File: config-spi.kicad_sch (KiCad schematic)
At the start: 29 parts, among them J3001 PinHeader_2x7_P2mm_SMD_Shroud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, Q3001 BSS138PW, Q3002 BSS138PW, SW3001 SW_KMR211NGLFS_SMD, SW3002 CVS-03B, U3001 S25FL128SAGNFI000, U3002 XC7K160T-FFG676

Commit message: Bump revision to 1.0.0
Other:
- title: LPDDR5 Test Board -> SO-DIMM DDR5 Tester

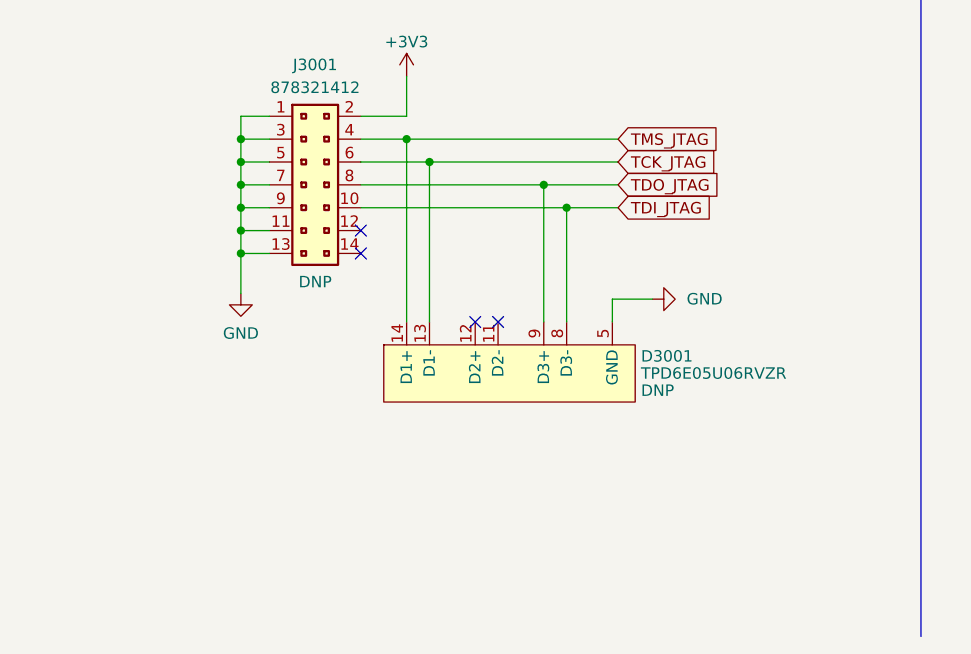
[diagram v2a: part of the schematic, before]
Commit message: Connect RFU, start improving interfaces and supply sheet, unify ESD protection
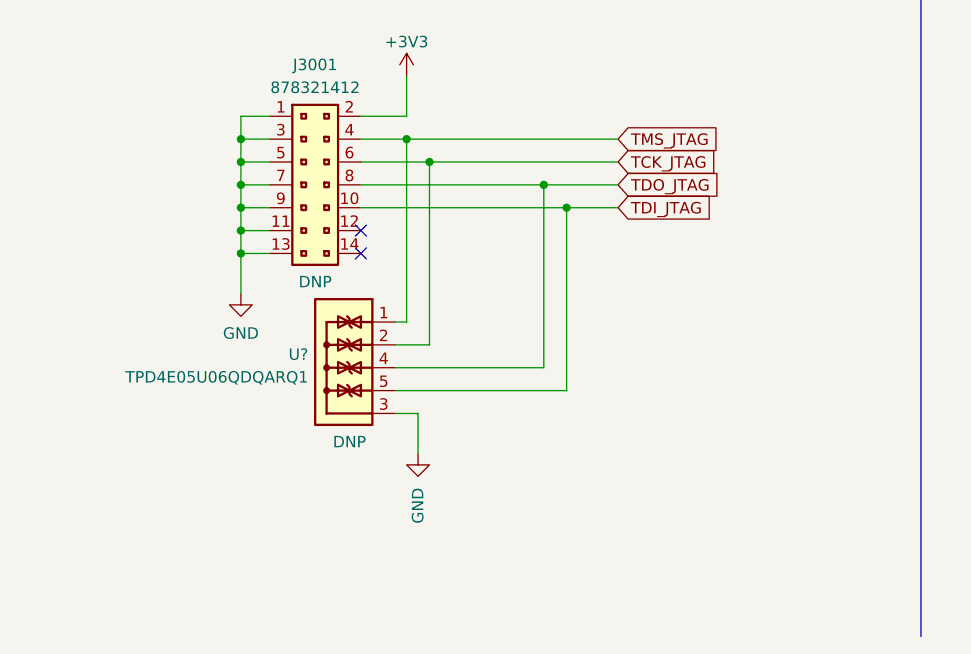
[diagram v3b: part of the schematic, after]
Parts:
- removed D3001: TPD6E05U06RVZR, sodimm-ddr5-tester-footprints:USON-14_3.5X1.3X0.5mm_P0.5mm, symbol sodimm-ddr5-tester:TPD6E05U06RVZR
- added U?: TPD4E05U06QDQARQ1, antmicro-footprints:USON-10_2.5x1mm_P0.5mm, symbol antmicroTVSDiodes:TPD4E05U06QDQARQ1
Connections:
- net GND: now also U?.3, U?.8
- net TCK_JTAG: now also U?.2, U?.9
- net TDI_JTAG: now also U?.5, U?.6
- net TDO_JTAG: now also U?.4, U?.7
- net TMS_JTAG: now also U?.1, U?.10
- no-connect marks 4 -> 2
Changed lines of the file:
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@@
   )
   (no_connect (at 50.165 242.57))
-  (no_connect (at 62.865 250.19))
-  (no_connect (at 65.405 250.19))
   (no_connect (at 50.165 240.03))
   (wire (pts (xy 111.125 88.9) (xy 111.125 92.075))
@@
     (stroke (width 0) (type default) (color 0 0 0 0))
   )
-  (wire (pts (xy 73.025 250.19) (xy 73.025 237.49))
+  (wire (pts (xy 73.025 237.49) (xy 73.025 257.81))
     (stroke (width 0) (type default) (color 0 0 0 0))
   )
@@
     (stroke (width 0) (type default) (color 0 0 0 0))
   )
-  (wire (pts (xy 57.785 250.19) (xy 57.785 232.41))
+  (wire (pts (xy 57.785 232.41) (xy 57.785 252.73))
     (stroke (width 0) (type default) (color 0 0 0 0))
   )
@@
     (stroke (width 0) (type default) (color 0 0 0 0))
   )
-  (wire (pts (xy 70.485 250.19) (xy 70.485 234.95))
+  (wire (pts (xy 70.485 234.95) (xy 70.485 255.27))
     (stroke (width 0) (type default) (color 0 0 0 0))
   )
@@
     (stroke (width 0) (type default) (color 0 0 0 0))
   )
-  (wire (pts (xy 78.105 247.65) (xy 82.55 247.65))
+  (wire (pts (xy 56.515 260.35) (xy 56.515 264.795))
     (stroke (width 0) (type default) (color 0 0 0 0))
   )
@@
     (stroke (width 0) (type default) (color 0 0 0 0))
   )
+  (wire (pts (xy 53.975 255.27) (xy 70.485 255.27))
+    (stroke (width 0) (type default) (color 0 0 0 0))
+  )
   (wire (pts (xy 50.165 229.87) (xy 55.245 229.87))
     (stroke (width 0) (type default) (color 0 0 0 0))
@@
     (stroke (width 0) (type default) (color 0 0 0 0))
   )
+  (wire (pts (xy 53.975 257.81) (xy 73.025 257.81))
+    (stroke (width 0) (type default) (color 0 0 0 0))
+  )
   (wire (pts (xy 128.905 88.9) (xy 128.905 92.075))
     (stroke (width 0) (type default) (color 0 0 0 0))
@@
     (stroke (width 0) (type default) (color 0 0 0 0))
   )
+  (wire (pts (xy 53.975 252.73) (xy 57.785 252.73))
+    (stroke (width 0) (type default) (color 0 0 0 0))
+  )
   (wire (pts (xy 224.79 258.445) (xy 252.095 258.445))
     (stroke (width 0) (type default) (color 0 0 0 0))
@@
     (stroke (width 0) (type default) (color 0 0 0 0))
   )
+  (wire (pts (xy 53.975 250.19) (xy 55.245 250.19))
+    (stroke (width 0) (type default) (color 0 0 0 0))
+  )
   (wire (pts (xy 73.025 100.965) (xy 73.025 102.87))
     (stroke (width 0) (type default) (color 0 0 0 0))
@@
     (stroke (width 0) (type default) (color 0 0 0 0))
   )
-  (wire (pts (xy 78.105 250.19) (xy 78.105 247.65))
+  (wire (pts (xy 53.975 260.35) (xy 56.515 260.35))
     (stroke (width 0) (type default) (color 0 0 0 0))
   )
@@
     (pin "1")
   )
-  (symbol (lib_id "sodimm-ddr5-tester:TPD6E05U06RVZR") (at 55.245 250.19 90) (mirror x) (unit 1)
-    (in_bom yes) (on_board yes)
-    (property "Reference" "D3001" (id 0) (at 81.28 254 90)
-      (effects (font (size 1.27 1.27)) (justify right))
-    )
-    (property "Value" "TPD6E05U06RVZR" (id 1) (at 81.28 255.905 90)
-      (effects (font (size 1.27 1.27) (thickness 0.15)) (justify right))
-    )
-    (property "Footprint" "sodimm-ddr5-tester-footprints:USON-14_3.5X1.3X0.5mm_P0.5mm" (id 2) (at 60.325 273.05 0)
-      (effects (font (size 1.27 1.27) (thickness 0.15)) (justify left bottom) hide)
-    )
-    (property "Datasheet" "http://www.ti.com/lit/ds/symlink/tpd6e05u06.pdf" (id 3) (at 62.865 273.05 0)
-      (effects (font (size 1.27 1.27) (thickness 0.15)) (justify left bottom) hide)
-    )
-    (property "MPN" "TPD6E05U06RVZR" (id 4) (at 65.405 273.05 0)
-      (effects (font (size 1.27 1.27) (thickness 0.15)) (justify left bottom) hide)
-    )
-    (property "Manufacturer" "Texas Instruments" (id 5) (at 67.945 273.05 0)
-      (effects (font (size 1.27 1.27) (thickness 0.15)) (justify left bottom) hide)
-    )
-    (property "Author" "Antmicro" (id 6) (at 70.485 273.05 0)
-      (effects (font (size 1.27 1.27) (thickness 0.15)) (justify left bottom) hide)
-    )
-    (property "License" "Apache-2.0" (id 7) (at 73.025 273.05 0)
-      (effects (font (size 1.27 1.27) (thickness 0.15)) (justify left bottom) hide)
-    )
-    (property "DNP" "DNP" (id 8) (at 81.28 257.81 90)
-      (effects (font (size 1.27 1.27)) (justify right))
-    )
-    (pin "1")
-    (pin "2")
-    (pin "3")
-    (pin "4")
-    (pin "6")
-    (pin "7")
-    (pin "10")
-    (pin "11")
-    (pin "12")
-    (pin "13")
-    (pin "14")
-    (pin "5")
-    (pin "8")
-    (pin "9")
-  )
-  (symbol (lib_id "sodimm-ddr5-tester:GND") (at 82.55 247.65 90) (unit 1)
+  (symbol (lib_id "sodimm-ddr5-tester:GND") (at 56.515 264.795 0) (unit 1)
     (in_bom yes) (on_board yes) (fields_autoplaced)
-    (property "Reference" "#PWR03004" (id 0) (at 88.9 247.65 0)
+    (property "Reference" "#PWR03004" (id 0) (at 56.515 271.145 0)
       (effects (font (size 1.27 1.27)) hide)
     )
-    (property "Value" "GND" (id 1) (at 86.36 247.6499 90)
+    (property "Value" "GND" (id 1) (at 56.5151 268.605 90)
       (effects (font (size 1.27 1.27)) (justify right))
     )
-    (property "Footprint" "" (id 2) (at 82.55 247.65 0)
+    (property "Footprint" "" (id 2) (at 56.515 264.795 0)
       (effects (font (size 1.27 1.27)) hide)
     )
-    (property "Datasheet" "" (id 3) (at 82.55 247.65 0)
+    (property "Datasheet" "" (id 3) (at 56.515 264.795 0)
       (effects (font (size 1.27 1.27)) hide)
     )
-    (property "Author" "Antmicro" (id 4) (at 90.17 238.76 0)
+    (property "Author" "Antmicro" (id 4) (at 65.405 272.415 0)
       (effects (font (size 1.27 1.27) (thickness 0.15)) (justify left bottom) hide)
     )
-    (property "License" "Apache-2.0" (id 5) (at 92.71 238.76 0)
+    (property "License" "Apache-2.0" (id 5) (at 65.405 274.955 0)
       (effects (font (size 1.27 1.27) (thickness 0.15)) (justify left bottom) hide)
     )
@@
     (pin "2")
   )
+  (symbol (lib_id "antmicroTVSDiodes:TPD4E05U06QDQARQ1") (at 53.975 250.19 0) (mirror y) (unit 1)
+    (in_bom yes) (on_board yes)
+    (property "Reference" "U?" (id 0) (at 44.323 253.8044 0)
+      (effects (font (size 1.27 1.27) (thickness 0.15)) (justify left))
+    )
+    (property "Value" "TPD4E05U06QDQARQ1" (id 1) (at 44.323 256.3281 0)
+      (effects (font (size 1.27 1.27) (thickness 0.15)) (justify left))
+    )
+    (property "Footprint" "antmicro-footprints:USON-10_2.5x1mm_P0.5mm" (id 2) (at 29.845 255.27 0)
+      (effects (font (size 1.27 1.27) (thickness 0.15)) (justify left bottom) hide)
+    )
+    (property "Datasheet" "https://www.ti.com/lit/ds/symlink/tpd4e05u06-q1.pdf?HQS=dis-mous-null-mousermode-dsf-pf-null-wwe&ts=1663591265741&ref_url=https%253A%252F%252Fwww.mouser.com%252F" (id 3) (at 29.845 257.81 0)
+      (effects (font (size 1.27 1.27) (thickness 0.15)) (justify left bottom) hide)
+    )
+    (property "Manufacturer" "Texas Instruments" (id 4) (at 29.845 260.35 0)
+      (effects (font (size 1.27 1.27) (thickness 0.15)) (justify left bottom) hide)
+    )
+    (property "MPN" "TPD4E05U06QDQARQ1" (id 5) (at 29.845 262.89 0)
+      (effects (font (size 1.27 1.27) (thickness 0.15)) (justify left bottom) hide)
+    )
+    (property "Author" "Antmicro" (id 6) (at 29.845 265.43 0)
+      (effects (font (size 1.27 1.27) (thickness 0.15)) (justify left bottom) hide)
+    )
+    (property "License" "Apache-2.0" (id 7) (at 29.845 267.97 0)
+      (effects (font (size 1.27 1.27) (thickness 0.15)) (justify left bottom) hide)
+    )
+    (property "DNP" "DNP" (id 8) (at 48.895 263.525 0))
+    (pin "1")
+    (pin "10")
+    (pin "2")
+    (pin "3")
+    (pin "4")
+    (pin "5")
+    (pin "6")
+    (pin "7")
+    (pin "8")
+    (pin "9")
+  )
   (symbol (lib_id "sodimm-ddr5-tester:SW_KMR211NGLFS_SMD") (at 255.27 129.54 270) (unit 1)

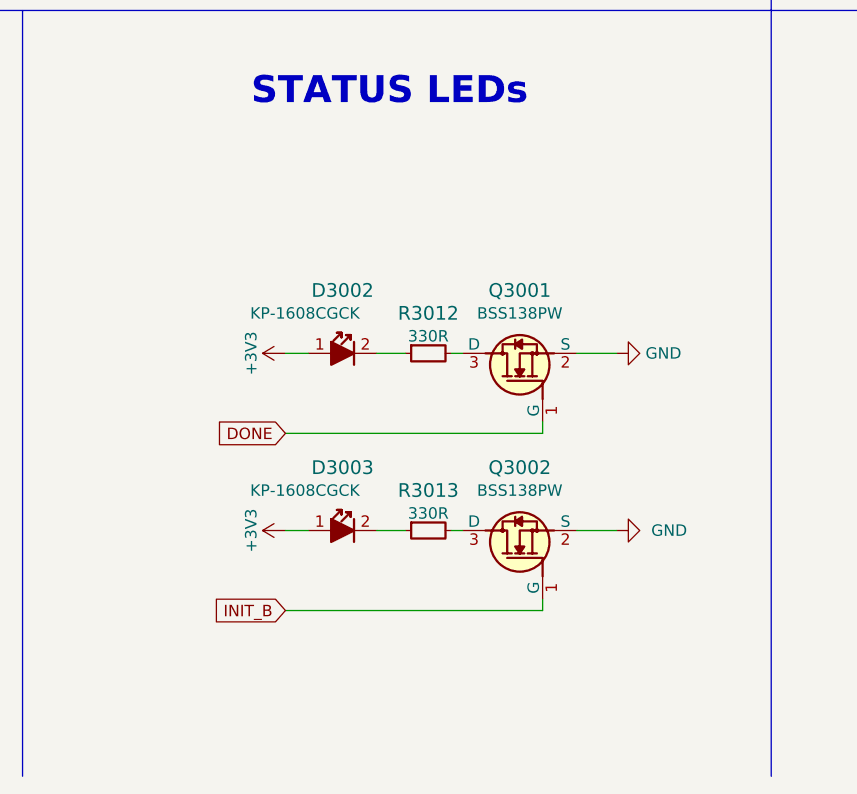
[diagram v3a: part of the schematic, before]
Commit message: Connect control and misc. signals, fix PCIe directions, rework I2C architecture, optimize DC-DC supply utilization
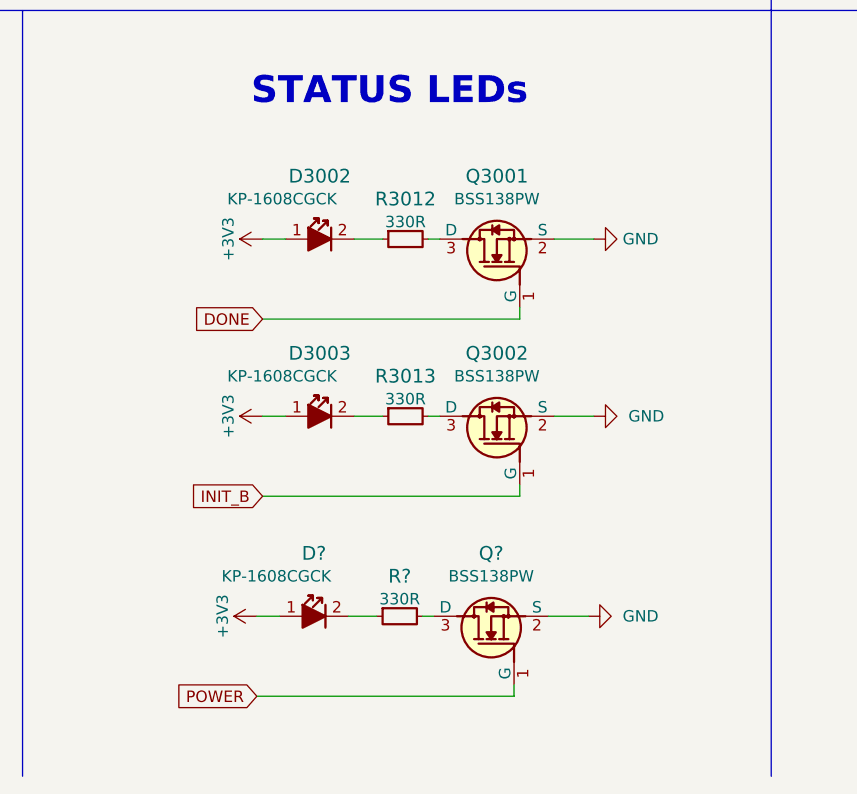
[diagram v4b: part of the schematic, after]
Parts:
- added D?: LED_G_0603_KP-1608CGCK, sodimm-ddr5-tester-footprints:LED_0603_1608Metric_G, symbol sodimm-ddr5-tester:LED_G_0603_KP-1608CGCK
- added Q?: BSS138PW, sodimm-ddr5-tester-footprints:SC70-3, symbol sodimm-ddr5-tester:BSS138PW
- added R?: R_330R_0402, sodimm-ddr5-tester-footprints:R_0402_1005Metric, symbol sodimm-ddr5-tester:R_330R_0402
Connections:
- net +3V3: now also D?.1
- net GND: now also Q?.2 (S)
- new net: D?.2, R?.1
- new net: Q?.3 (D), R?.2
- new net POWER: Q?.1 (G)
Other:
- moved on the sheet: D3002, D3003, Q3001, Q3002, R3012, R3013

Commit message: Sync new components with PCB
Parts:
- gave numbers to parts that had none: 4
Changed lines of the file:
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@@
   (symbol (lib_id "sodimm-ddr5-tester:R_330R_0402") (at 151.765 267.335 0) (unit 1)
     (in_bom yes) (on_board yes)
-    (property "Reference" "R?" (id 0) (at 154.305 262.89 0)
+    (property "Reference" "R3004" (id 0) (at 154.305 262.89 0)
       (effects (font (size 1.524 1.524)))
     )
@@
   (symbol (lib_id "sodimm-ddr5-tester:+3V3") (at 138.43 267.335 90) (unit 1)
     (in_bom yes) (on_board yes)
-    (property "Reference" "#PWR?" (id 0) (at 142.24 267.335 0)
+    (property "Reference" "#PWR0149" (id 0) (at 142.24 267.335 0)
       (effects (font (size 1.27 1.27)) hide)
     )
@@
   (symbol (lib_id "sodimm-ddr5-tester:LED_G_0603_KP-1608CGCK") (at 140.97 267.335 0) (unit 1)
     (in_bom yes) (on_board yes)
-    (property "Reference" "D?" (id 0) (at 144.78 260.35 0)
+    (property "Reference" "D3001" (id 0) (at 144.78 260.35 0)
       (effects (font (size 1.524 1.524)))
     )
@@
   (symbol (lib_id "antmicroTVSDiodes:TPD4E05U06QDQARQ1") (at 53.975 250.19 0) (mirror y) (unit 1)
     (in_bom yes) (on_board yes)
-    (property "Reference" "U?" (id 0) (at 44.323 253.8044 0)
+    (property "Reference" "U3003" (id 0) (at 44.323 253.8044 0)
       (effects (font (size 1.27 1.27) (thickness 0.15)) (justify left))
     )
@@
   (symbol (lib_id "sodimm-ddr5-tester:GND") (at 175.26 267.335 90) (unit 1)
     (in_bom yes) (on_board yes) (fields_autoplaced)
-    (property "Reference" "#PWR?" (id 0) (at 181.61 267.335 0)
+    (property "Reference" "#PWR0150" (id 0) (at 181.61 267.335 0)
       (effects (font (size 1.27 1.27)) hide)
     )
@@
   (symbol (lib_id "sodimm-ddr5-tester:BSS138PW") (at 167.005 274.955 90) (unit 1)
     (in_bom yes) (on_board yes)
-    (property "Reference" "Q?" (id 0) (at 164.465 260.35 90)
+    (property "Reference" "Q3003" (id 0) (at 164.465 260.35 90)
       (effects (font (size 1.524 1.524)))
     )

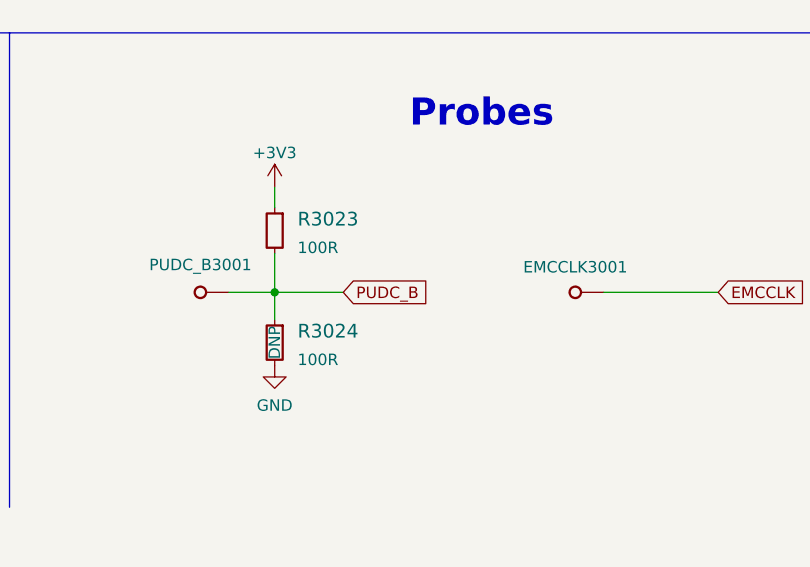
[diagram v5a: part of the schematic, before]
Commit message: Optimize BOM, replace obsolete parts, improve manufacturing attributes
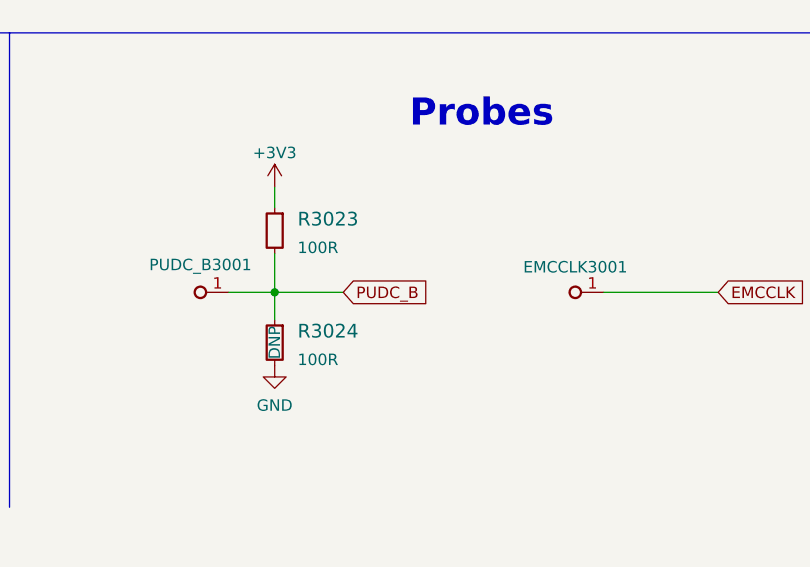
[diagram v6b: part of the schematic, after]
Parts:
- EMCCLK3001, PUDC_B3001: footprint sodimm-ddr5-tester-footprints:Testpoint_smd_1mm -> antmicro-footprints:TP_SMD_1mm; symbol sodimm-ddr5-tester:TP_1mm_SMD -> antmicroTestPoints:TP_1mm_SMD
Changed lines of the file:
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@@
     (pin "1")
   )
-  (symbol (lib_id "sodimm-ddr5-tester:TP_1mm_SMD") (at 324.104 228.854 180) (unit 1)
+  (symbol (lib_id "antmicroTestPoints:TP_1mm_SMD") (at 324.104 228.854 180) (unit 1)
     (in_bom yes) (on_board yes) (fields_autoplaced)
     (property "Reference" "PUDC_B3001" (id 0) (at 320.929 225.806 0))
@@
       (effects (font (size 1.27 1.27) (thickness 0.15)) (justify left bottom) hide)
     )
-    (property "Footprint" "sodimm-ddr5-tester-footprints:Testpoint_smd_1mm" (id 2) (at 308.864 218.694 0)
+    (property "Footprint" "antmicro-footprints:TP_SMD_1mm" (id 2) (at 308.864 218.694 0)
       (effects (font (size 1.27 1.27) (thickness 0.15)) (justify left bottom) hide)
     )
@@
     (pin "1")
   )
-  (symbol (lib_id "sodimm-ddr5-tester:TP_1mm_SMD") (at 365.76 228.854 180) (unit 1)
+  (symbol (lib_id "antmicroTestPoints:TP_1mm_SMD") (at 365.76 228.854 180) (unit 1)
     (in_bom yes) (on_board yes) (fields_autoplaced)
     (property "Reference" "EMCCLK3001" (id 0) (at 362.585 226.06 0))
@@
       (effects (font (size 1.27 1.27) (thickness 0.15)) (justify left bottom) hide)
     )
-    (property "Footprint" "sodimm-ddr5-tester-footprints:Testpoint_smd_1mm" (id 2) (at 350.52 218.694 0)
+    (property "Footprint" "antmicro-footprints:TP_SMD_1mm" (id 2) (at 350.52 218.694 0)
       (effects (font (size 1.27 1.27) (thickness 0.15)) (justify left bottom) hide)
     )
